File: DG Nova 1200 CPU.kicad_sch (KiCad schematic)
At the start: 205 parts, among them Q1 MPS3640, U1 74LS11???, U10 74LS20, U100 045, U101 74LS04, U102 74LS179, U103 74LS179, U105 74LS179, U106 74LS179, U107 74LS179, U108 74LS179, U109 74LS00, U11 74LS03, U110 74LS20, U111 74LS10, U112 74LS51, U113 74LS114, U114 74LS51, U115 74LS179, U116 74LS157, U117 74LS181, U118 74LS00, U119 74LS170, U12 74LS00, U120 8264, U121 74LS157, U122 74LS179, U123 8225, U124 8225, U125 8264, U13 045, U14 74LS20, U15 74LS20, U16 74LS04, U17 74LS179, U18 74LS20, U19 74LS00, U2 74LS74, U20 74LS74, U21 74LS00, U22 74LS04, U23 74LS179, U24 74LS51, U25 74LS139, U26 74LS04, U27 74LS04, U28 74LS179, U29 74LS179, U3 74LS00, U30 82S23, U31 82S23, U32 74LS179, U33 74LS179, U34 045, U35 74LS10, U36 74LS00, U37 74LS179, U38 74LS179, U39 74LS179, U4 045, U40 74LS179, U41 045, U42 74LS179, U43 74H54, U44 74LS51, U45 74LS51, U46 74H54, U47 74H54, U48 045, U49 74LS03, U5 74LS04, U50 74LS10, U51 74LS139, U52 74LS139, U53 045, U54 74LS179, U55 74LS51, U56 74LS20, U57 74LS00, U58 045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

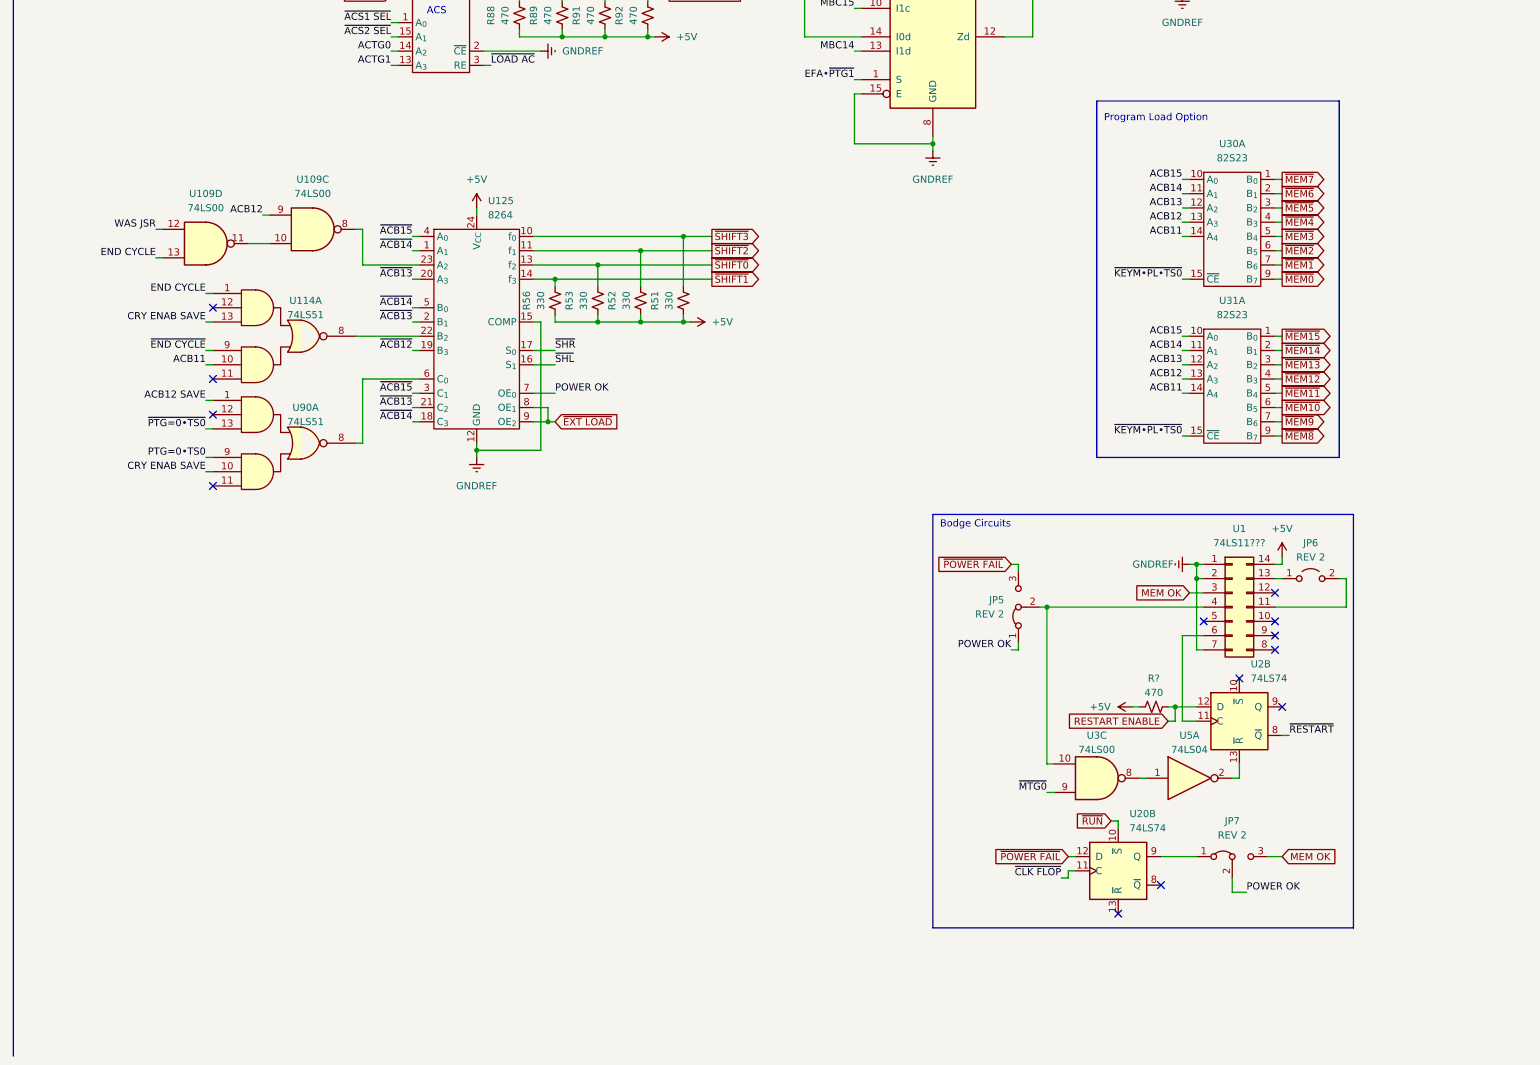
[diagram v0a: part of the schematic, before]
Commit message: Finished documenting Restart on Lock functionality
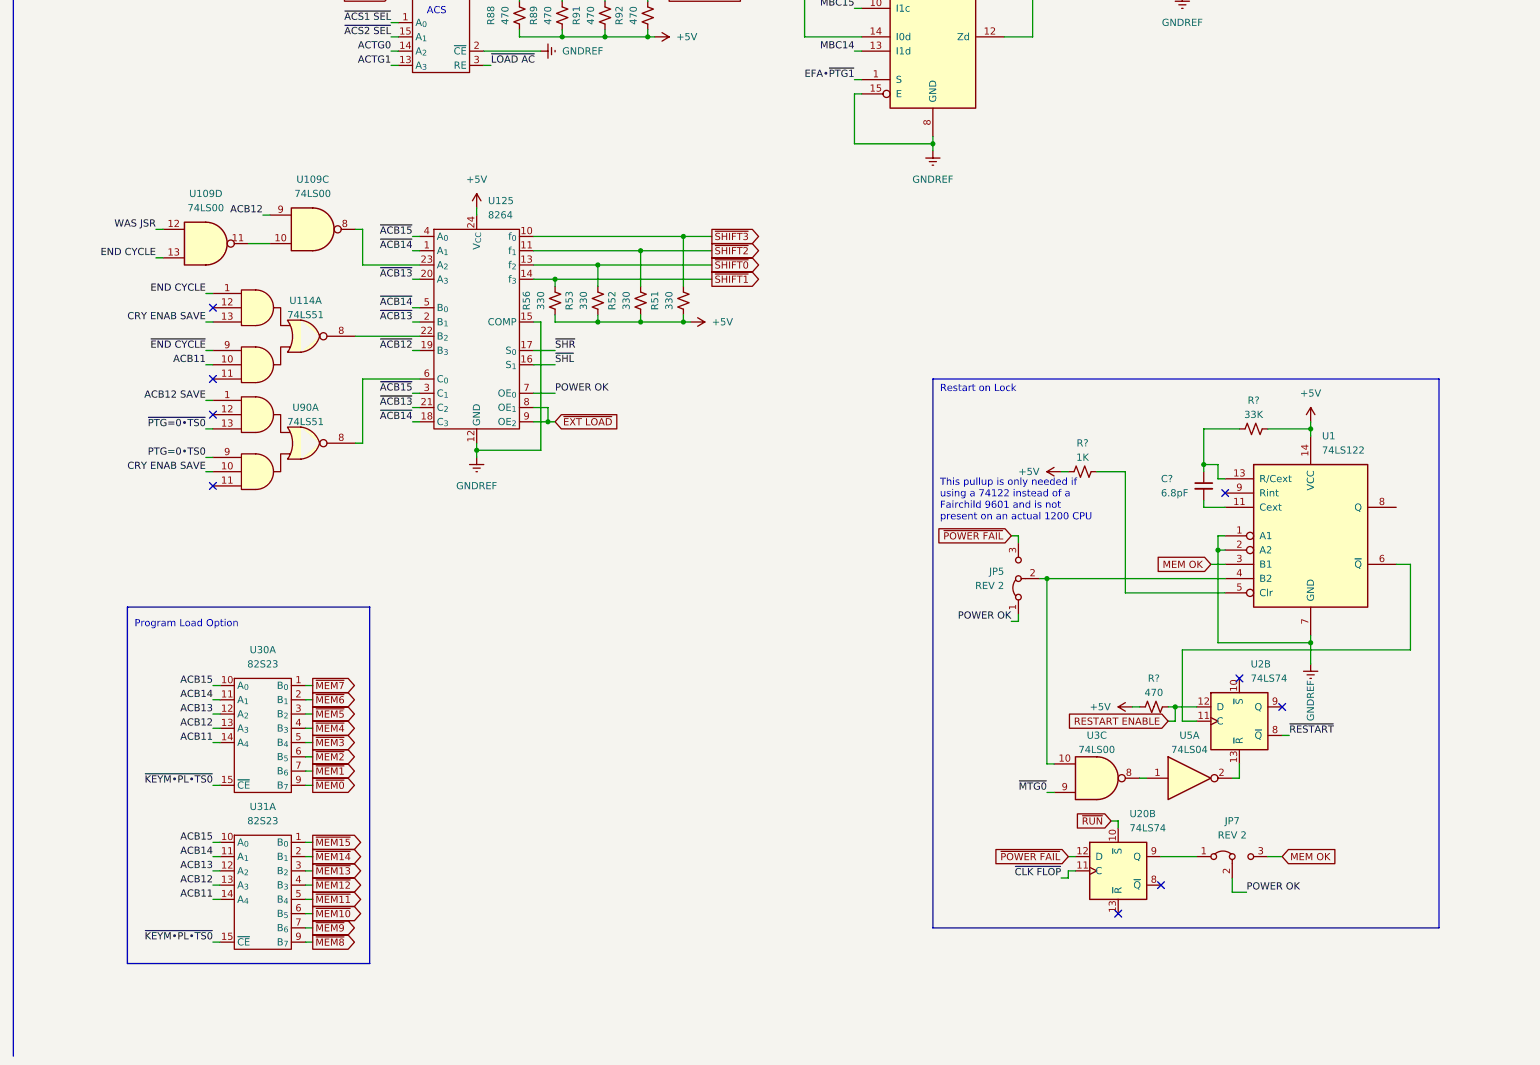
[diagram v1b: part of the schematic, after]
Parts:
- removed JP6: REV 2, symbol Jumper:Jumper_2_Open
- removed U1: 74LS11???, symbol Connector_Generic:Conn_02x07_Counter_Clockwise
- added C?: 6.8pF, symbol Device:C_Small
- added R?: 1K, symbol Device:R_Small_US
- added R?: 33K, symbol Device:R_Small_US
- added U1: 74LS122, symbol 74xx:74LS122
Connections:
- net +5V: now also R?.1, R?.2, U1.14 (VCC)
- net GNDREF: now also U1.1 (A1), U1.2 (A2), U1.7 (GND)
- net MEM OK: now also U1.3 (B1)
- net at JP5.2 (C), U3.10: now also U1.4 (B2)
- net at U2.11 (C): now also U1.6 (~{Q})
- new net: C?.2, U1.11 (Cext)
- new net: C?.1, R?.1, U1.13 (R/Cext)
- new net: R?.2, U1.5 (Clr)
- no-connect marks 73 -> 69
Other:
- note added: "Restart on Lock"
- note added: "This pullup is only needed if using a 74122 instead of a Fairchild 9601 and is not present on an actual 1200 CPU"
- note removed: "Bodge Circuits"
- moved on the sheet: JP5, U30A, U31A

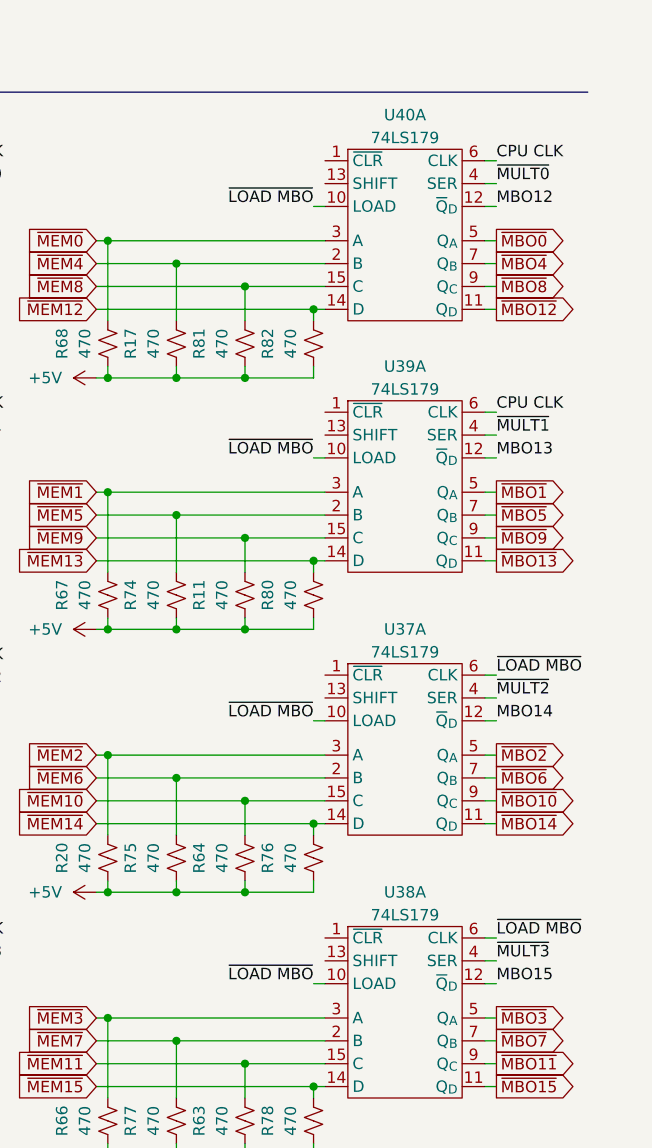
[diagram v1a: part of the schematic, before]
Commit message: Fixed typo on U37, U38, U39, U40
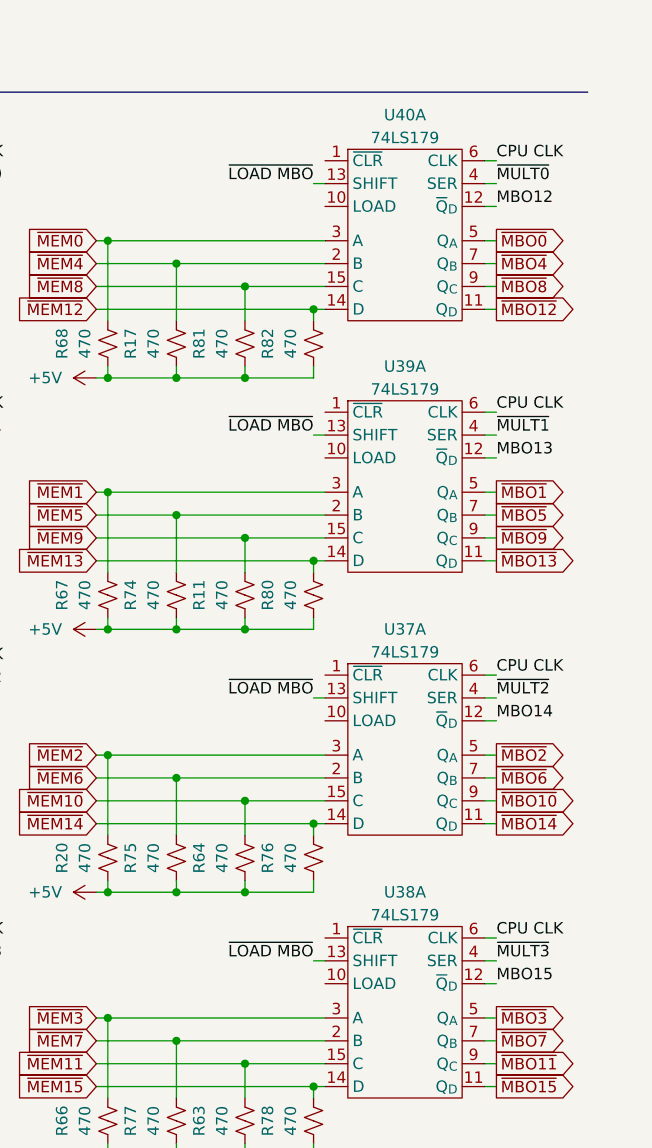
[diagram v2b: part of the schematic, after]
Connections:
- net CPU CLK: now also U37.6 (CLK), U38.6 (CLK)
- net ~{LOAD MBO}: now also U37.13 (SHIFT), U38.13 (SHIFT), U39.13 (SHIFT), U40.13 (SHIFT); no longer U37.10 (LOAD), U37.6 (CLK), U38.10 (LOAD), U38.6 (CLK), U39.10 (LOAD), U40.10 (LOAD)
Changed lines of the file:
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@@
     (stroke (width 0) (type default) (color 0 0 0 0))
   )
-  (wire (pts (xy 820.42 266.7) (xy 821.69 266.7))
-    (stroke (width 0) (type default) (color 0 0 0 0))
-  )
   (wire (pts (xy 718.82 285.75) (xy 718.82 289.56))
     (stroke (width 0) (type default) (color 0 0 0 0))
@@
     (stroke (width 0) (type default) (color 0 0 0 0))
   )
+  (wire (pts (xy 820.42 321.31) (xy 821.69 321.31))
+    (stroke (width 0) (type default) (color 0 0 0 0))
+  )
   (wire (pts (xy 133.35 204.47) (xy 133.35 212.09))
     (stroke (width 0) (type default) (color 0 0 0 0))
@@
     (stroke (width 0) (type default) (color 0 0 0 0))
   )
+  (wire (pts (xy 820.42 292.1) (xy 821.69 292.1))
+    (stroke (width 0) (type default) (color 0 0 0 0))
+  )
   (wire (pts (xy 182.88 448.31) (xy 184.15 448.31))
     (stroke (width 0) (type default) (color 0 0 0 0))
@@
     (stroke (width 0) (type default) (color 0 0 0 0))
   )
-  (wire (pts (xy 820.42 294.64) (xy 821.69 294.64))
-    (stroke (width 0) (type default) (color 0 0 0 0))
-  )
   (wire (pts (xy 713.74 151.13) (xy 715.01 151.13))
     (stroke (width 0) (type default) (color 0 0 0 0))
@@
     (stroke (width 0) (type default) (color 0 0 0 0))
   )
-  (wire (pts (xy 820.42 323.85) (xy 821.69 323.85))
-    (stroke (width 0) (type default) (color 0 0 0 0))
-  )
   (wire (pts (xy 725.17 53.34) (xy 725.17 55.88))
     (stroke (width 0) (type default) (color 0 0 0 0))
@@
     (stroke (width 0) (type default) (color 0 0 0 0))
   )
+  (wire (pts (xy 820.42 264.16) (xy 821.69 264.16))
+    (stroke (width 0) (type default) (color 0 0 0 0))
+  )
   (wire (pts (xy 488.95 349.25) (xy 513.08 349.25))
     (stroke (width 0) (type default) (color 0 0 0 0))
@@
     (stroke (width 0) (type default) (color 0 0 0 0))
   )
+  (wire (pts (xy 820.42 350.52) (xy 821.69 350.52))
+    (stroke (width 0) (type default) (color 0 0 0 0))
+  )
   (wire (pts (xy 176.53 288.29) (xy 177.8 288.29))
     (stroke (width 0) (type default) (color 0 0 0 0))
@@
     (stroke (width 0) (type default) (color 0 0 0 0))
   )
-  (wire (pts (xy 820.42 353.06) (xy 821.69 353.06))
-    (stroke (width 0) (type default) (color 0 0 0 0))
-  )
   (wire (pts (xy 679.45 45.72) (xy 680.72 45.72))
     (stroke (width 0) (type default) (color 0 0 0 0))
@@
     (effects (font (size 1.27 1.27)) (justify left bottom))
   )
+  (label "CPU CLK" (at 840.74 318.77 0)
+    (effects (font (size 1.27 1.27)) (justify left bottom))
+  )
   (label "~{PTG5 ENAB}" (at 363.22 214.63 180)
     (effects (font (size 1.27 1.27)) (justify right bottom))
@@
     (effects (font (size 1.27 1.27)) (justify right bottom))
   )
-  (label "~{LOAD MBO}" (at 820.42 323.85 180)
+  (label "~{LOAD MBO}" (at 820.42 321.31 180)
     (effects (font (size 1.27 1.27)) (justify right bottom))
   )
@@
     (effects (font (size 1.27 1.27)) (justify right bottom))
   )
+  (label "CPU CLK" (at 840.74 347.98 0)
+    (effects (font (size 1.27 1.27)) (justify left bottom))
+  )
   (label "~{RESTART}" (at 111.76 427.99 180)
     (effects (font (size 1.27 1.27)) (justify right bottom))
@@
     (effects (font (size 1.27 1.27)) (justify right bottom))
   )
-  (label "~{LOAD MBO}" (at 840.74 347.98 0)
-    (effects (font (size 1.27 1.27)) (justify left bottom))
-  )
   (label "~{IR7}" (at 193.04 309.88 180)
     (effects (font (size 1.27 1.27)) (justify right bottom))
@@
     (effects (font (size 1.27 1.27)) (justify right bottom))
   )
-  (label "~{LOAD MBO}" (at 820.42 353.06 180)
+  (label "~{LOAD MBO}" (at 820.42 350.52 180)
     (effects (font (size 1.27 1.27)) (justify right bottom))
   )
@@
     (effects (font (size 1.27 1.27)) (justify right bottom))
   )
-  (label "~{LOAD MBO}" (at 820.42 266.7 180)
+  (label "~{LOAD MBO}" (at 820.42 264.16 180)
     (effects (font (size 1.27 1.27)) (justify right bottom))
   )
@@
     (effects (font (size 1.27 1.27)) (justify right bottom))
   )
-  (label "~{LOAD MBO}" (at 840.74 318.77 0)
-    (effects (font (size 1.27 1.27)) (justify left bottom))
-  )
   (label "SKIP" (at 789.94 154.94 0)
     (effects (font (size 1.27 1.27)) (justify left bottom))
@@
     (effects (font (size 1.27 1.27)) (justify right bottom))
   )
-  (label "~{LOAD MBO}" (at 820.42 294.64 180)
+  (label "~{LOAD MBO}" (at 820.42 292.1 180)
     (effects (font (size 1.27 1.27)) (justify right bottom))
   )

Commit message: Fixes
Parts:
- removed JP1: REV 2, symbol Jumper:Jumper_2_Open
- added JP6: REV 2, symbol Jumper:Jumper_3_Bridged12
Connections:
- net ~{MULT0 is gone; now on net ~{MULT0}: R90.2, U119.10 (Q1), U120.10 (f_{0})
- net KEY: now also U82.2
- net MEM OK: now also JP7.1 (A); no longer JP7.3 (B)
- net ~{KEY SEEN}: now also U2.6 (~{Q}), U21.1
- net ~{RESTART}: now also JP6.3 (B)
- net at U20.9 (Q): now also JP7.3 (B); no longer JP7.1 (A)
- net at U28.1 (~{CLR}): now also JP6.2 (C)
- net RESTART: now reaches U2.9 (Q)
- net RESTART: now also U82.1
- net at U82.3: now also JP6.1 (A)
- no-connect marks 69 -> 65
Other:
- note added: "Assume all unconnected inputs are pulled high internally. This is a property of the 74S series logic family used by DG at the time. Note that the 74LS series does NOT have this property and any replacement parts should include external pullups."
- moved on the sheet: U82A

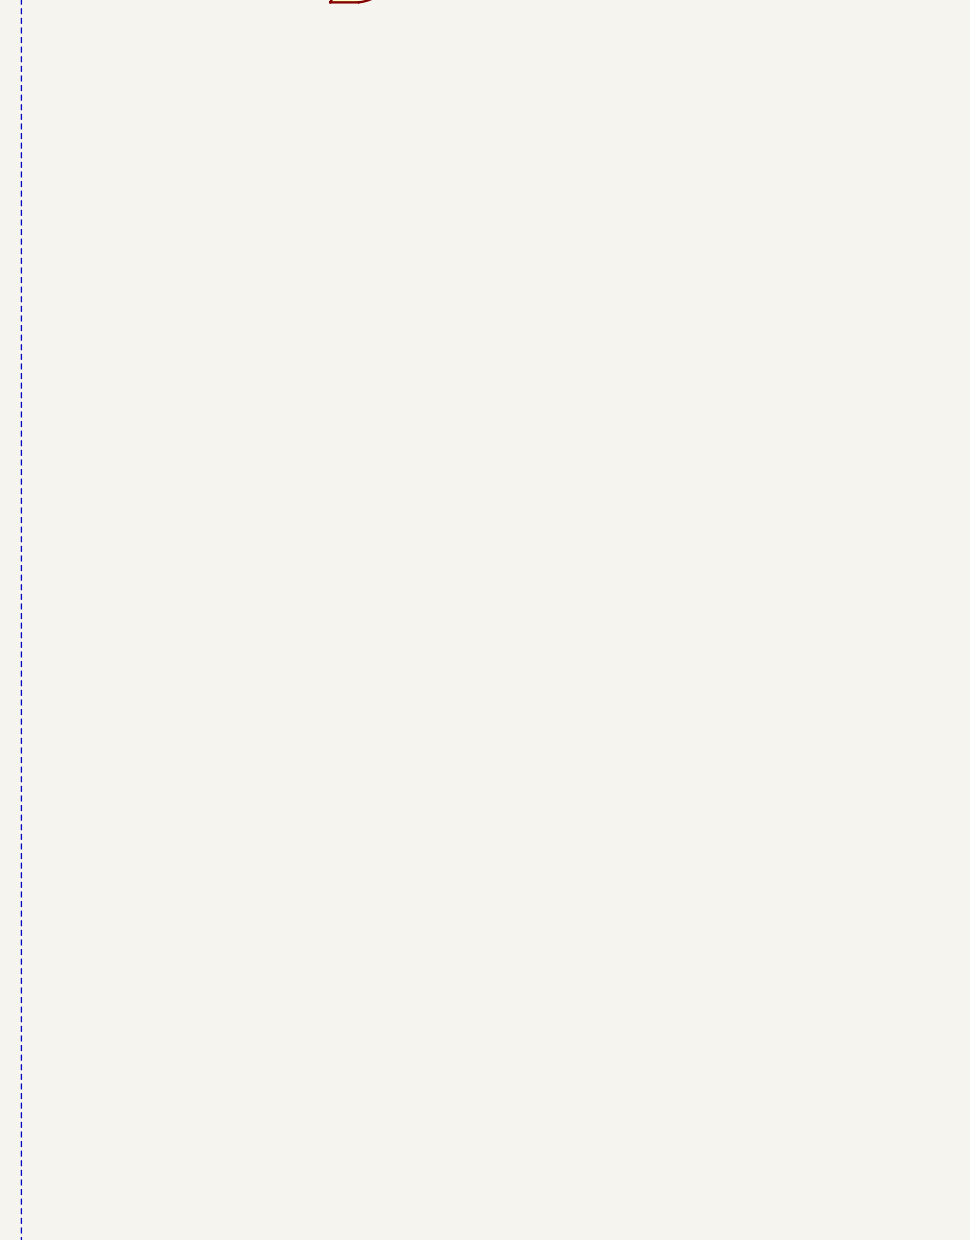
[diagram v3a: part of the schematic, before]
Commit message: Add data bus pullups
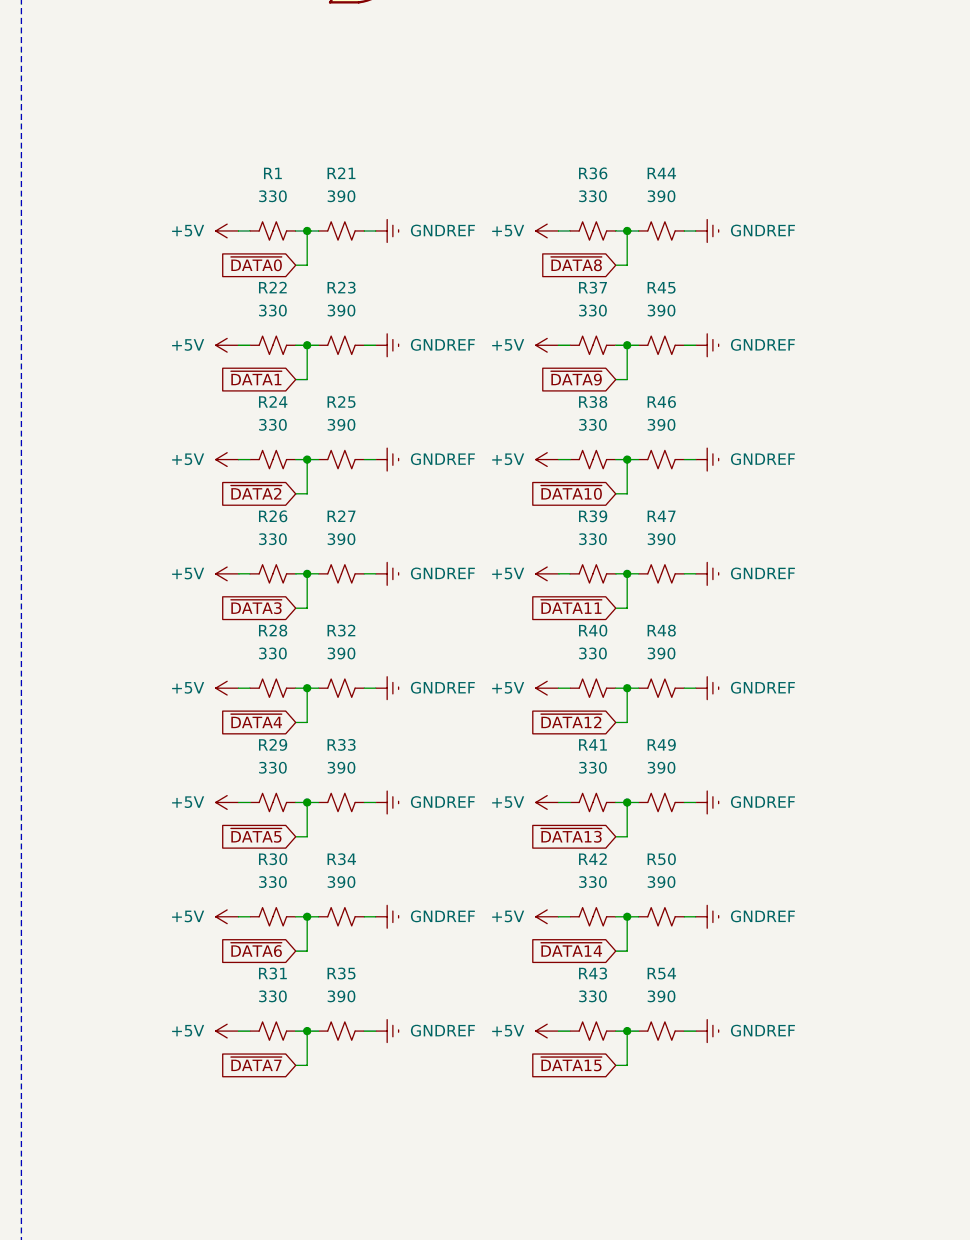
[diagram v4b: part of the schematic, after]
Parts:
- added R1, R22, R24, R26, R28, R29, R30, R31, R36, R37, R38, R39, R40, R41, R42, R43: 330, symbol Device:R_Small_US
- added R21, R23, R25, R27, R32, R33, R34, R35, R44, R45, R46, R47, R48, R49, R50, R54: 390, symbol Device:R_Small_US
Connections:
- net +5V: now also R1.1, R22.1, R24.1, R26.1, R28.1, R29.1, R30.1, R31.1, R36.1, R37.1, R38.1, R39.1, R40.1, R41.1, R42.1, R43.1
- net GNDREF: now also R21.2, R23.2, R25.2, R27.2, R32.2, R33.2, R34.2, R35.2, R44.2, R45.2, R46.2, R47.2, R48.2, R49.2, R50.2, R54.2
- new net ~{DATA0}: R1.2, R21.1
- new net ~{DATA10}: R38.2, R46.1
- new net ~{DATA11}: R39.2, R47.1
- new net ~{DATA12}: R40.2, R48.1
- new net ~{DATA13}: R41.2, R49.1
- new net ~{DATA14}: R42.2, R50.1
- new net ~{DATA15}: R43.2, R54.1
- new net ~{DATA1}: R22.2, R23.1
- new net ~{DATA2}: R24.2, R25.1
- new net ~{DATA3}: R26.2, R27.1
- new net ~{DATA4}: R28.2, R32.1
- new net ~{DATA5}: R29.2, R33.1
- new net ~{DATA6}: R30.2, R34.1
- new net ~{DATA7}: R31.2, R35.1
- new net ~{DATA8}: R36.2, R44.1
- new net ~{DATA9}: R37.2, R45.1

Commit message: Fixed an issue where I swapped 2 gates
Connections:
- net TEST SKIP SET: now also U102.2 (B), U86.3
- net at U62.6: now also U41.5; no longer U41.12
- net at U43.8, U83.3: now also U41.12; no longer U41.5
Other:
- moved on the sheet: U41B, U41D, U82C, U83B
